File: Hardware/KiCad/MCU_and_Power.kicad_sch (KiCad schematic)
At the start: 43 parts

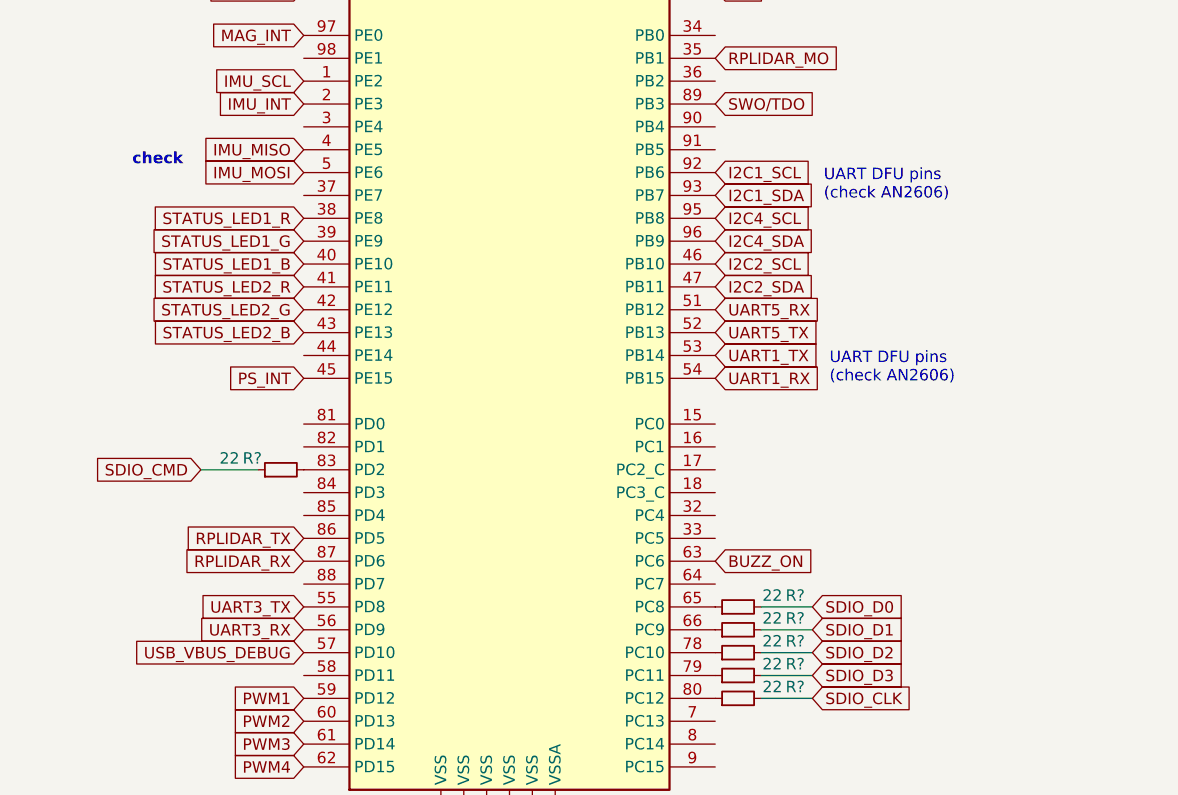
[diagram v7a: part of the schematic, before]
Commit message: Switched some RX and TX pins
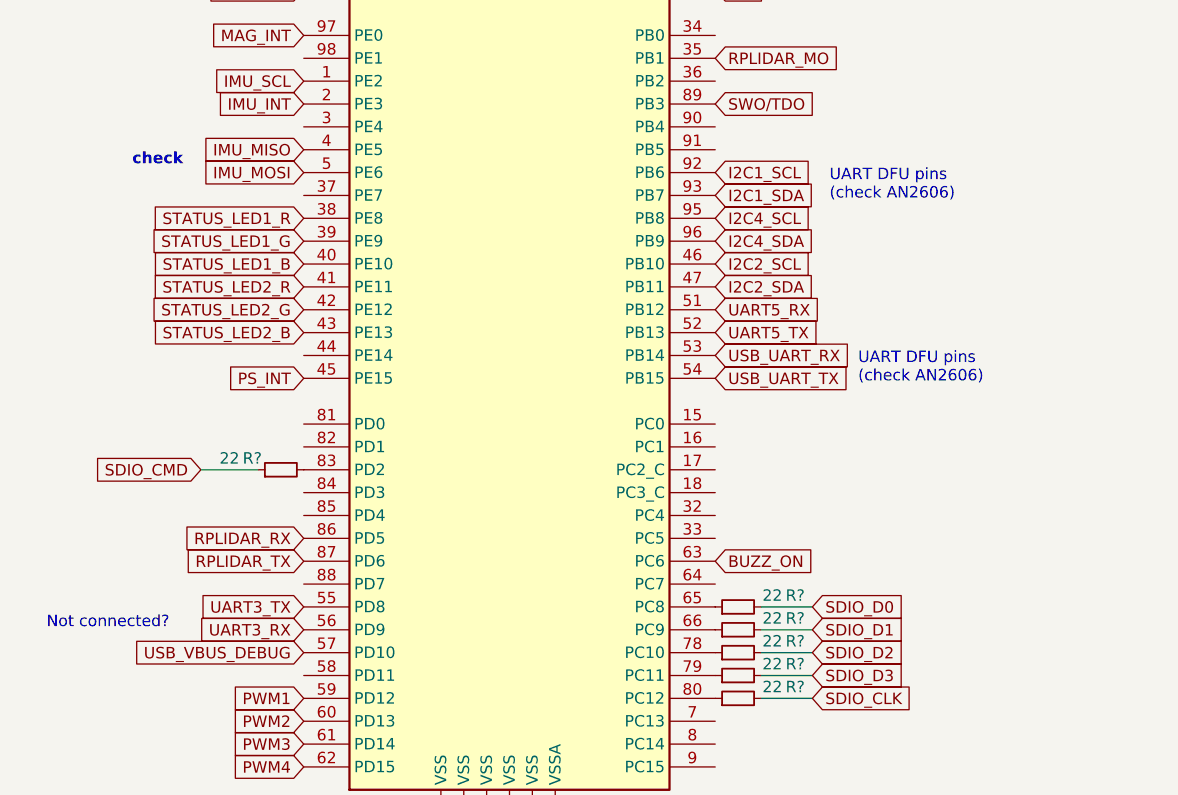
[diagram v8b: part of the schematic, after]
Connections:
- net RPLIDAR_RX: now also U?.86 (PD5); no longer U?.87 (PD6)
- net RPLIDAR_TX: now also U?.87 (PD6); no longer U?.86 (PD5)
- net UART1_RX renamed USB_UART_TX
- net UART1_TX renamed USB_UART_RX
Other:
- note added: "Not connected?"
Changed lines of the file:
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@@
     (effects (font (size 2 2)) (justify left bottom))
+  )
+  (text "Not connected?" (at 34.925 159.385 0)
+    (effects (font (size 1.27 1.27)) (justify left bottom))
   )
   (text "Vref+ filtering" (at 234.315 92.71 0)
     (effects (font (size 2 2)) (justify left bottom))
   )
-  (text "UART DFU pins \n(check AN2606)" (at 121.92 132.08 0)
+  (text "UART DFU pins \n(check AN2606)" (at 125.095 132.08 0)
     (effects (font (size 1.27 1.27)) (justify left bottom))
   )
@@
     (effects (font (size 1.27 1.27)) (justify left bottom))
   )
-  (text "UART DFU pins \n(check AN2606)" (at 121.285 111.76 0)
+  (text "UART DFU pins \n(check AN2606)" (at 121.92 111.76 0)
     (effects (font (size 1.27 1.27)) (justify left bottom))
   )
@@
     )
   )
+  (global_label "USB_UART_RX" (shape input) (at 109.22 128.905 0) (fields_autoplaced)
+    (effects (font (size 1.27 1.27)) (justify left))
+    (property "Intersheet References" "${INTERSHEET_REFS}" (id 0) (at 124.5145 128.8256 0)
+      (effects (font (size 1.27 1.27)) (justify left) hide)
+    )
+  )
   (global_label "STATUS_LED2_G" (shape input) (at 63.5 123.825 180) (fields_autoplaced)
     (effects (font (size 1.27 1.27)) (justify right))
@@
     )
   )
-  (global_label "RPLIDAR_TX" (shape input) (at 63.5 149.225 180) (fields_autoplaced)
-    (effects (font (size 1.27 1.27)) (justify right))
-    (property "Intersheet References" "${INTERSHEET_REFS}" (id 0) (at 50.1407 149.1456 0)
-      (effects (font (size 1.27 1.27)) (justify right) hide)
-    )
-  )
   (global_label "USB_ID" (shape input) (at 121.285 75.565 0) (fields_autoplaced)
     (effects (font (size 1.27 1.27)) (justify left))
@@
     )
   )
+  (global_label "RPLIDAR_RX" (shape input) (at 63.5 149.225 180) (fields_autoplaced)
+    (effects (font (size 1.27 1.27)) (justify right))
+    (property "Intersheet References" "${INTERSHEET_REFS}" (id 0) (at 49.8383 149.1456 0)
+      (effects (font (size 1.27 1.27)) (justify right) hide)
+    )
+  )
   (global_label "IMU_MOSI" (shape input) (at 63.5 108.585 180) (fields_autoplaced)
     (effects (font (size 1.27 1.27)) (justify right))
@@
     )
   )
-  (global_label "UART1_TX" (shape input) (at 109.22 128.905 0) (fields_autoplaced)
-    (effects (font (size 1.27 1.27)) (justify left))
-    (property "Intersheet References" "${INTERSHEET_REFS}" (id 0) (at 120.6441 128.8256 0)
-      (effects (font (size 1.27 1.27)) (justify left) hide)
-    )
-  )
   (global_label "TDI" (shape input) (at 109.22 88.265 0) (fields_autoplaced)
     (effects (font (size 1.27 1.27)) (justify left))
@@
     )
   )
+  (global_label "USB_UART_TX" (shape input) (at 109.22 131.445 0) (fields_autoplaced)
+    (effects (font (size 1.27 1.27)) (justify left))
+    (property "Intersheet References" "${INTERSHEET_REFS}" (id 0) (at 124.2121 131.3656 0)
+      (effects (font (size 1.27 1.27)) (justify left) hide)
+    )
+  )
   (global_label "USB_VBUS_PROG" (shape input) (at 121.285 73.025 0) (fields_autoplaced)
     (effects (font (size 1.27 1.27)) (justify left))
@@
     )
   )
+  (global_label "RPLIDAR_TX" (shape input) (at 63.5 151.765 180) (fields_autoplaced)
+    (effects (font (size 1.27 1.27)) (justify right))
+    (property "Intersheet References" "${INTERSHEET_REFS}" (id 0) (at 50.1407 151.6856 0)
+      (effects (font (size 1.27 1.27)) (justify right) hide)
+    )
+  )
   (global_label "I2C2_SDA" (shape input) (at 109.22 121.285 0) (fields_autoplaced)
     (effects (font (size 1.27 1.27)) (justify left))
@@
     )
   )
-  (global_label "UART1_RX" (shape input) (at 109.22 131.445 0) (fields_autoplaced)
-    (effects (font (size 1.27 1.27)) (justify left))
-    (property "Intersheet References" "${INTERSHEET_REFS}" (id 0) (at 120.9464 131.3656 0)
-      (effects (font (size 1.27 1.27)) (justify left) hide)
-    )
-  )
   (global_label "STATUS_LED1_G" (shape input) (at 63.5 116.205 180) (fields_autoplaced)
     (effects (font (size 1.27 1.27)) (justify right))
@@
     )
   )
-  (global_label "RPLIDAR_RX" (shape input) (at 63.5 151.765 180) (fields_autoplaced)
-    (effects (font (size 1.27 1.27)) (justify right))
-    (property "Intersheet References" "${INTERSHEET_REFS}" (id 0) (at 49.8383 151.6856 0)
-      (effects (font (size 1.27 1.27)) (justify right) hide)
-    )
-  )
